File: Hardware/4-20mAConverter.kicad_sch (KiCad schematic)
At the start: 26 parts, among them J11 Screw_Terminal, Q17 NPN, U15 LM324, U16 LM317_TO-252, U17 TL431

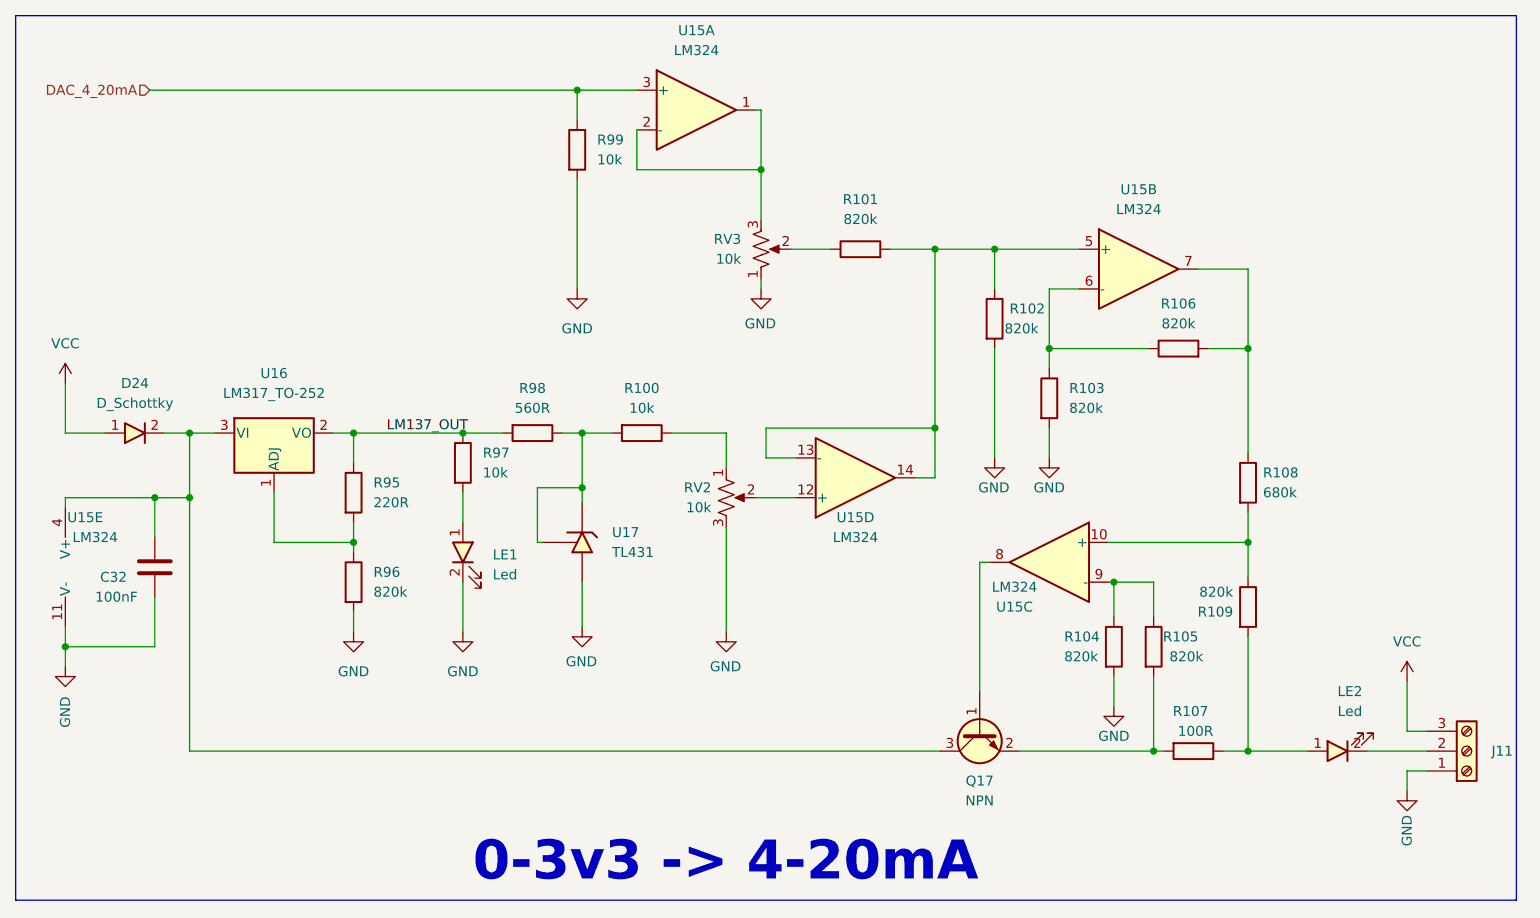
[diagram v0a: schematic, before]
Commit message: fix block 4-20mA
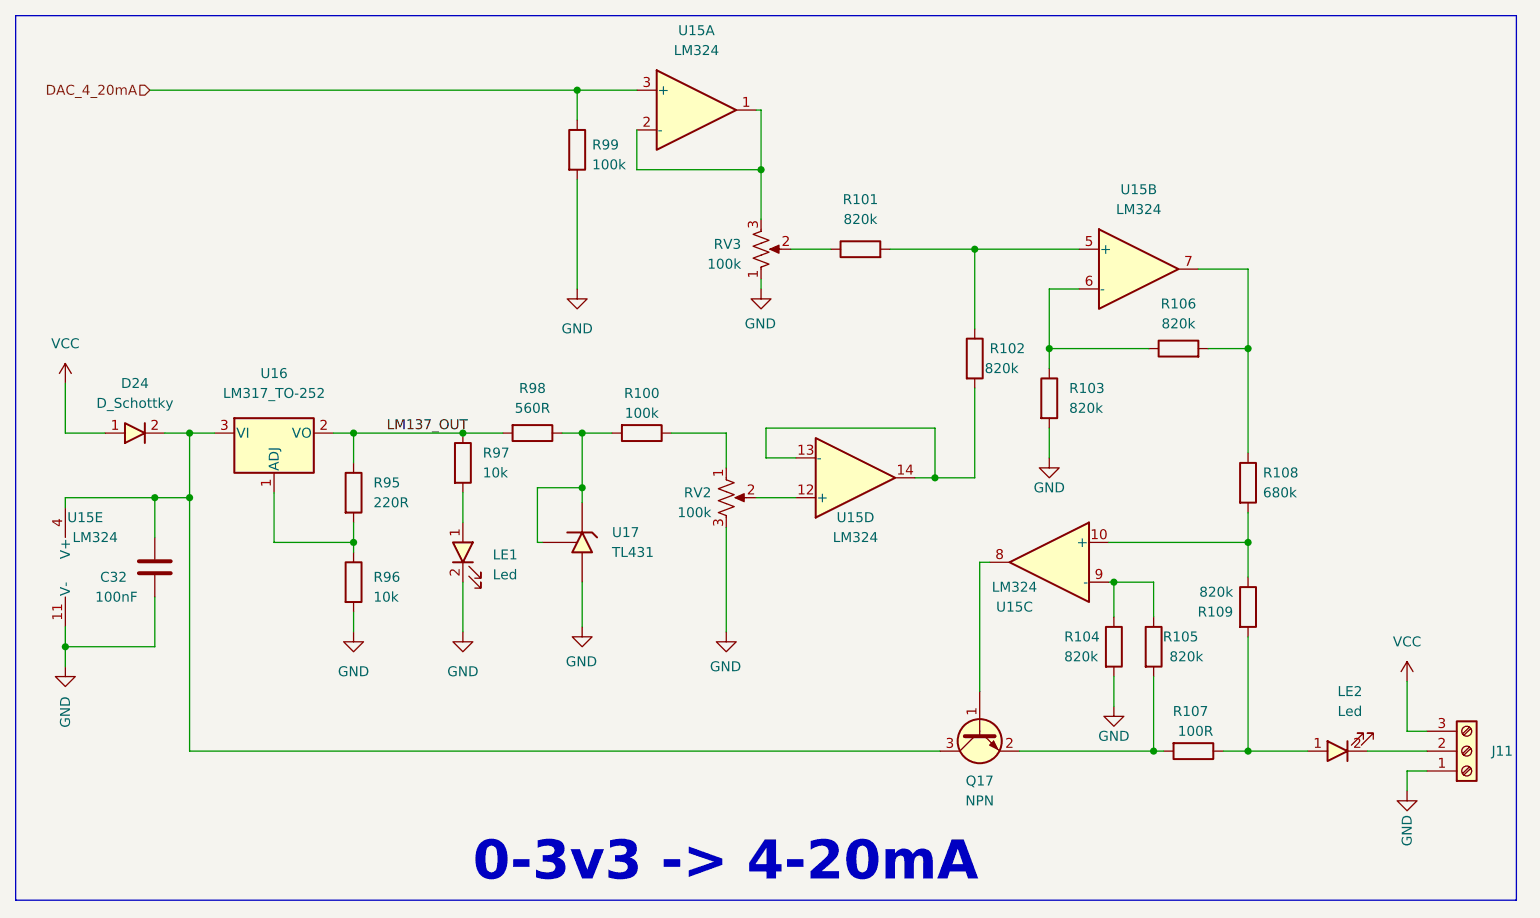
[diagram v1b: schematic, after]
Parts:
- R100, R99, RV2, RV3: value 10k -> 100k
- R96: value 820k -> 10k
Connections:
- net GND: no longer R102.2
- net at R101.2, R102.1, U15.5 (+): no longer U15.13 (-), U15.14
- new net: R102.2, U15.13 (-), U15.14
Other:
- moved on the sheet: R102
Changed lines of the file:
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@@
   (junction (at 92.075 28.575) (diameter 0) (color 0 0 0 0)
   )
-  (junction (at 137.795 71.755) (diameter 0) (color 0 0 0 0)
-  )
   (junction (at 92.71 72.39) (diameter 0) (color 0 0 0 0)
   )
+  (junction (at 137.795 78.105) (diameter 0) (color 0 0 0 0)
+  )
   (junction (at 160.655 91.44) (diameter 0) (color 0 0 0 0)
   )
@@
   (junction (at 42.545 80.645) (diameter 0) (color 0 0 0 0)
   )
+  (junction (at 142.875 48.895) (diameter 0) (color 0 0 0 0)
+  )
   (junction (at 42.545 72.39) (diameter 0) (color 0 0 0 0)
   )
@@
   (junction (at 115.57 38.735) (diameter 0) (color 0 0 0 0)
   )
-  (junction (at 145.415 48.895) (diameter 0) (color 0 0 0 0)
-  )
-  (junction (at 137.795 48.895) (diameter 0) (color 0 0 0 0)
-  )
   (junction (at 152.4 61.595) (diameter 0) (color 0 0 0 0)
   )
@@
     (stroke (width 0) (type default))
   )
+  (wire (pts (xy 142.875 48.895) (xy 156.21 48.895))
+    (stroke (width 0) (type default))
+  )
   (wire (pts (xy 77.47 72.39) (xy 82.55 72.39))
     (stroke (width 0) (type default))
@@
     (stroke (width 0) (type default))
   )
+  (wire (pts (xy 142.875 78.105) (xy 137.795 78.105))
+    (stroke (width 0) (type default))
+  )
   (wire (pts (xy 116.205 75.565) (xy 116.205 71.755))
     (stroke (width 0) (type default))
@@
     (stroke (width 0) (type default))
   )
+  (wire (pts (xy 142.875 66.675) (xy 142.875 78.105))
+    (stroke (width 0) (type default))
+  )
   (wire (pts (xy 38.1 93.345) (xy 38.1 99.695))
     (stroke (width 0) (type default))
@@
     (stroke (width 0) (type default))
   )
-  (wire (pts (xy 145.415 48.895) (xy 145.415 53.975))
+  (wire (pts (xy 142.875 48.895) (xy 142.875 59.055))
     (stroke (width 0) (type default))
   )
@@
     (stroke (width 0) (type default))
   )
-  (wire (pts (xy 137.795 48.895) (xy 137.795 71.755))
-    (stroke (width 0) (type default))
-  )
   (wire (pts (xy 92.075 40.005) (xy 92.075 53.975))
     (stroke (width 0) (type default))
@@
     (stroke (width 0) (type default))
   )
-  (wire (pts (xy 145.415 48.895) (xy 156.21 48.895))
-    (stroke (width 0) (type default))
-  )
   (wire (pts (xy 144.78 88.9) (xy 143.51 88.9))
     (stroke (width 0) (type default))
@@
     (stroke (width 0) (type default))
   )
-  (wire (pts (xy 132.08 48.895) (xy 137.795 48.895))
-    (stroke (width 0) (type default))
-  )
   (wire (pts (xy 160.655 103.505) (xy 160.655 107.315))
     (stroke (width 0) (type default))
@@
     (stroke (width 0) (type default))
   )
-  (wire (pts (xy 145.415 48.895) (xy 137.795 48.895))
-    (stroke (width 0) (type default))
-  )
-  (wire (pts (xy 145.415 61.595) (xy 145.415 75.565))
+  (wire (pts (xy 132.08 48.895) (xy 142.875 48.895))
     (stroke (width 0) (type default))
   )
@@
   (symbol (lib_id "Device:R") (at 92.075 36.195 0) (unit 1)
     (in_bom yes) (on_board yes) (dnp no) (fields_autoplaced)
-    (property "Reference" "R99" (at 94.615 34.9249 0)
-      (effects (font (size 1.27 1.27)) (justify left))
-    )
-    (property "Value" "10k" (at 94.615 37.4649 0)
+    (property "Reference" "R99" (at 93.98 35.56 0)
+      (effects (font (size 1.27 1.27)) (justify left))
+    )
+    (property "Value" "100k" (at 93.98 38.1 0)
       (effects (font (size 1.27 1.27)) (justify left))
     )
@@
     )
   )
-  (symbol (lib_id "power:GND") (at 145.415 75.565 0) (unit 1)
-    (in_bom yes) (on_board yes) (dnp no)
-    (property "Reference" "#PWR0157" (at 145.415 81.915 0)
-      (effects (font (size 1.27 1.27)) hide)
-    )
-    (property "Value" "GND" (at 147.32 79.375 0)
-      (effects (font (size 1.27 1.27)) (justify right))
-    )
-    (property "Footprint" "" (at 145.415 75.565 0)
-      (effects (font (size 1.27 1.27)) hide)
-    )
-    (property "Datasheet" "" (at 145.415 75.565 0)
-      (effects (font (size 1.27 1.27)) hide)
-    )
-    (pin "1")
-    (instances
-      (project "dongtam"
-        (path "/6833aec4-3d1d-4261-9b3e-f0452b565dd3/20e0764d-b27c-4f4c-b032-197976a30834"
-          (reference "#PWR0157") (unit 1)
-        )
-      )
-    )
-  )
   (symbol (lib_id "power:VCC") (at 198.12 104.14 0) (unit 1)
     (in_bom yes) (on_board yes) (dnp no) (fields_autoplaced)
@@
   (symbol (lib_id "Device:R") (at 63.5 91.44 0) (unit 1)
     (in_bom yes) (on_board yes) (dnp no) (fields_autoplaced)
-    (property "Reference" "R96" (at 66.04 90.1699 0)
-      (effects (font (size 1.27 1.27)) (justify left))
-    )
-    (property "Value" "820k" (at 66.04 92.7099 0)
+    (property "Reference" "R96" (at 66.04 90.805 0)
+      (effects (font (size 1.27 1.27)) (justify left))
+    )
+    (property "Value" "10k" (at 66.04 93.345 0)
       (effects (font (size 1.27 1.27)) (justify left))
     )
@@
   (symbol (lib_id "Device:R_Potentiometer_US") (at 115.57 48.895 0) (mirror x) (unit 1)
     (in_bom yes) (on_board yes) (dnp no) (fields_autoplaced)
-    (property "Reference" "RV3" (at 113.03 47.6249 0)
-      (effects (font (size 1.27 1.27)) (justify right))
-    )
-    (property "Value" "10k" (at 113.03 50.1649 0)
+    (property "Reference" "RV3" (at 113.03 48.26 0)
+      (effects (font (size 1.27 1.27)) (justify right))
+    )
+    (property "Value" "100k" (at 113.03 50.8 0)
       (effects (font (size 1.27 1.27)) (justify right))
     )
@@
   (symbol (lib_id "Device:R") (at 100.33 72.39 270) (unit 1)
     (in_bom yes) (on_board yes) (dnp no) (fields_autoplaced)
-    (property "Reference" "R100" (at 100.33 66.675 90)
-      (effects (font (size 1.27 1.27)))
-    )
-    (property "Value" "10k" (at 100.33 69.215 90)
+    (property "Reference" "R100" (at 100.33 67.31 90)
+      (effects (font (size 1.27 1.27)))
+    )
+    (property "Value" "100k" (at 100.33 69.85 90)
       (effects (font (size 1.27 1.27)))
     )
@@
   (symbol (lib_id "Device:R_Potentiometer_US") (at 111.125 80.645 0) (unit 1)
     (in_bom yes) (on_board yes) (dnp no) (fields_autoplaced)
-    (property "Reference" "RV2" (at 109.22 79.3749 0)
-      (effects (font (size 1.27 1.27)) (justify right))
-    )
-    (property "Value" "10k" (at 109.22 81.9149 0)
+    (property "Reference" "RV2" (at 109.22 80.01 0)
+      (effects (font (size 1.27 1.27)) (justify right))
+    )
+    (property "Value" "100k" (at 109.22 82.55 0)
       (effects (font (size 1.27 1.27)) (justify right))
     )
@@
     )
   )
-  (symbol (lib_id "Device:R") (at 145.415 57.785 0) (unit 1)
-    (in_bom yes) (on_board yes) (dnp no)
-    (property "Reference" "R102" (at 147.32 56.515 0)
-      (effects (font (size 1.27 1.27)) (justify left))
-    )
-    (property "Value" "820k" (at 146.685 59.055 0)
-      (effects (font (size 1.27 1.27)) (justify left))
-    )
-    (property "Footprint" "IVS_FOOTPRINTS:R0603" (at 143.637 57.785 90)
-      (effects (font (size 1.27 1.27)) hide)
-    )
-    (property "Datasheet" "~" (at 145.415 57.785 0)
-      (effects (font (size 1.27 1.27)) hide)
-    )
+  (symbol (lib_id "Device:R") (at 142.875 62.865 0) (unit 1)
+    (in_bom yes) (on_board yes) (dnp no)
+    (property "Reference" "R102" (at 144.78 61.595 0)
+      (effects (font (size 1.27 1.27)) (justify left))
+    )
+    (property "Value" "820k" (at 144.145 64.135 0)
+      (effects (font (size 1.27 1.27)) (justify left))
+    )
+    (property "Footprint" "IVS_FOOTPRINTS:R0603" (at 141.097 62.865 90)
+      (effects (font (size 1.27 1.27)) hide)
+    )
+    (property "Datasheet" "~" (at 142.875 62.865 0)
+      (effects (font (size 1.27 1.27)) hide)
+    )

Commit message: layout PCB part 1
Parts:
- J11: footprint IVS_FOOTPRINTS:HT - 3.96mm - 3pin -> IVS_FOOTPRINTS:Terminal_HT-P3.96mm-3P-Vertical-Pluggable
- LE1: footprint IVS_FOOTPRINTS:LED0805 -> IVS_FOOTPRINTS:LED0603
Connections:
- net GND: now also RV3.3; no longer RV3.1
- net at U15.1, U15.2 (-): now also RV3.1; no longer RV3.3

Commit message: layout part 2
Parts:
- U15: footprint IVS_FOOTPRINTS:TSSOP14 -> IVS_FOOTPRINTS:SOIC14
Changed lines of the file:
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@@
       (effects (font (size 1.27 1.27)))
     )
-    (property "Footprint" "IVS_FOOTPRINTS:TSSOP14" (at 106.045 28.575 0)
+    (property "Footprint" "IVS_FOOTPRINTS:SOIC14" (at 106.045 28.575 0)
       (effects (font (size 1.27 1.27)) hide)
     )
@@
       (effects (font (size 1.27 1.27)))
     )
-    (property "Footprint" "IVS_FOOTPRINTS:TSSOP14" (at 126.365 80.645 0)
+    (property "Footprint" "IVS_FOOTPRINTS:SOIC14" (at 126.365 80.645 0)
       (effects (font (size 1.27 1.27)) hide)
     )
@@
       (effects (font (size 1.27 1.27)))
     )
-    (property "Footprint" "IVS_FOOTPRINTS:TSSOP14" (at 27.94 86.995 0)
+    (property "Footprint" "IVS_FOOTPRINTS:SOIC14" (at 27.94 86.995 0)
       (effects (font (size 1.27 1.27)) hide)
     )
@@
       (effects (font (size 1.27 1.27)))
     )
-    (property "Footprint" "IVS_FOOTPRINTS:TSSOP14" (at 162.56 48.895 0)
+    (property "Footprint" "IVS_FOOTPRINTS:SOIC14" (at 162.56 48.895 0)
       (effects (font (size 1.27 1.27)) hide)
     )
@@
       (effects (font (size 1.27 1.27)))
     )
-    (property "Footprint" "IVS_FOOTPRINTS:TSSOP14" (at 153.67 86.36 0)
-      (effects (font (size 1.27 1.27)) hide)
-    )
+    (property "Footprint" "IVS_FOOTPRINTS:SOIC14" (at 153.67 86.36 0)
+      (effects (font (size 1.27 1.27)) hide)
+    )

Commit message: Complete board
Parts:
- D24: value D_Schottky -> 1N4007
- J11: value Screw_Terminal -> HT3.96mm-3P
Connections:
- net LM137_IN: now reaches C32.1, D24.2, Q17.3 (C), U15.4 (V+), U16.3 (VI)
- net TransB: now reaches Q17.1 (B), U15.8
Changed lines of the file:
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@@
     (effects (font (size 5 5) (thickness 1) bold) (justify left bottom))
+  )
+  (label "LM137_IN" (at 59.69 113.03 180) (fields_autoplaced)
+    (effects (font (size 1.27 1.27)) (justify right bottom))
+  )
+  (label "TransB" (at 143.51 102.87 180) (fields_autoplaced)
+    (effects (font (size 1.27 1.27)) (justify right bottom))
   )
   (label "LM137_OUT" (at 78.105 72.39 180) (fields_autoplaced)
@@
   (symbol (lib_id "IVS_SYMBOLS:D_Diode") (at 36.83 72.39 180) (unit 1)
     (in_bom yes) (on_board yes) (dnp no) (fields_autoplaced)
-    (property "Reference" "D24" (at 35.56 66.04 0)
-      (effects (font (size 1.27 1.27)))
-    )
-    (property "Value" "D_Schottky" (at 35.56 68.58 0)
+    (property "Reference" "D24" (at 35.56 67.31 0)
+      (effects (font (size 1.27 1.27)))
+    )
+    (property "Value" "1N4007" (at 35.56 69.85 0)
       (effects (font (size 1.27 1.27)))
     )
@@
       (effects (font (size 1.27 1.27)) (justify left))
     )
-    (property "Value" "Screw_Terminal" (at 208.28 111.7601 0)
+    (property "Value" "HT3.96mm-3P" (at 208.28 111.7601 0)
       (effects (font (size 1.27 1.27)) (justify left) hide)
     )

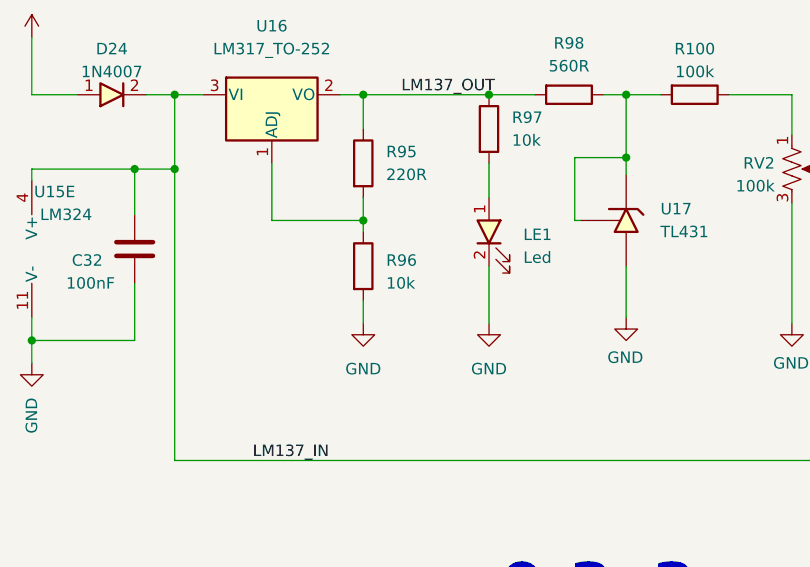
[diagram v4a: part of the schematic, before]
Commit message: complete PCB & fix SCH
fix pull push resistor Pin A, B RS485
diode RTC PCF8564
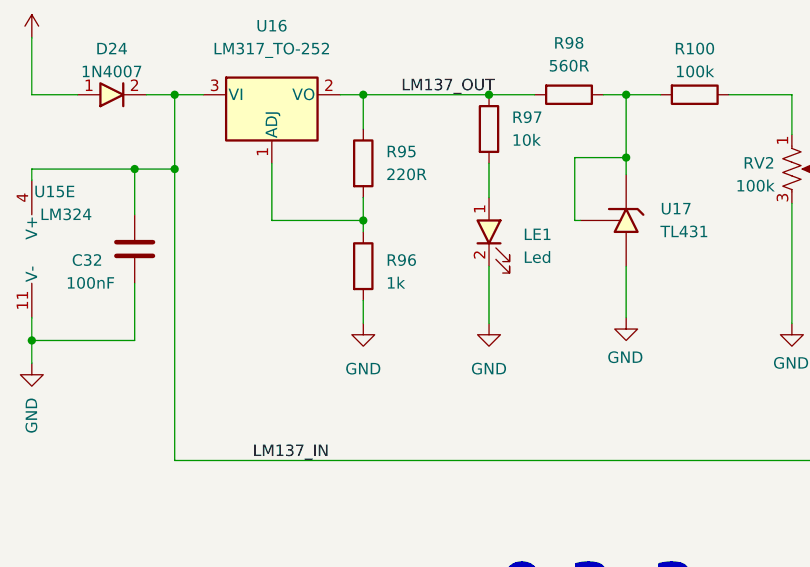
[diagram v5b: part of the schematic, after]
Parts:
- R96: value 10k -> 1k
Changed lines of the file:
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@@
       (effects (font (size 1.27 1.27)) (justify left))
     )
-    (property "Value" "10k" (at 66.04 93.345 0)
+    (property "Value" "1k" (at 66.04 93.345 0)
       (effects (font (size 1.27 1.27)) (justify left))
     )
